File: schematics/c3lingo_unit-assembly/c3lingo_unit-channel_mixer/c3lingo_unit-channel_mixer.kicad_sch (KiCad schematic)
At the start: 83 parts, among them J301 Interconnect, J302 PowerSupply, J303 I/O, SW301 OnAir_X, SW302 Mute_X, U301 LM833-N, U302 LM339, U303 LM339, U304 LM339, U305 LM833-N

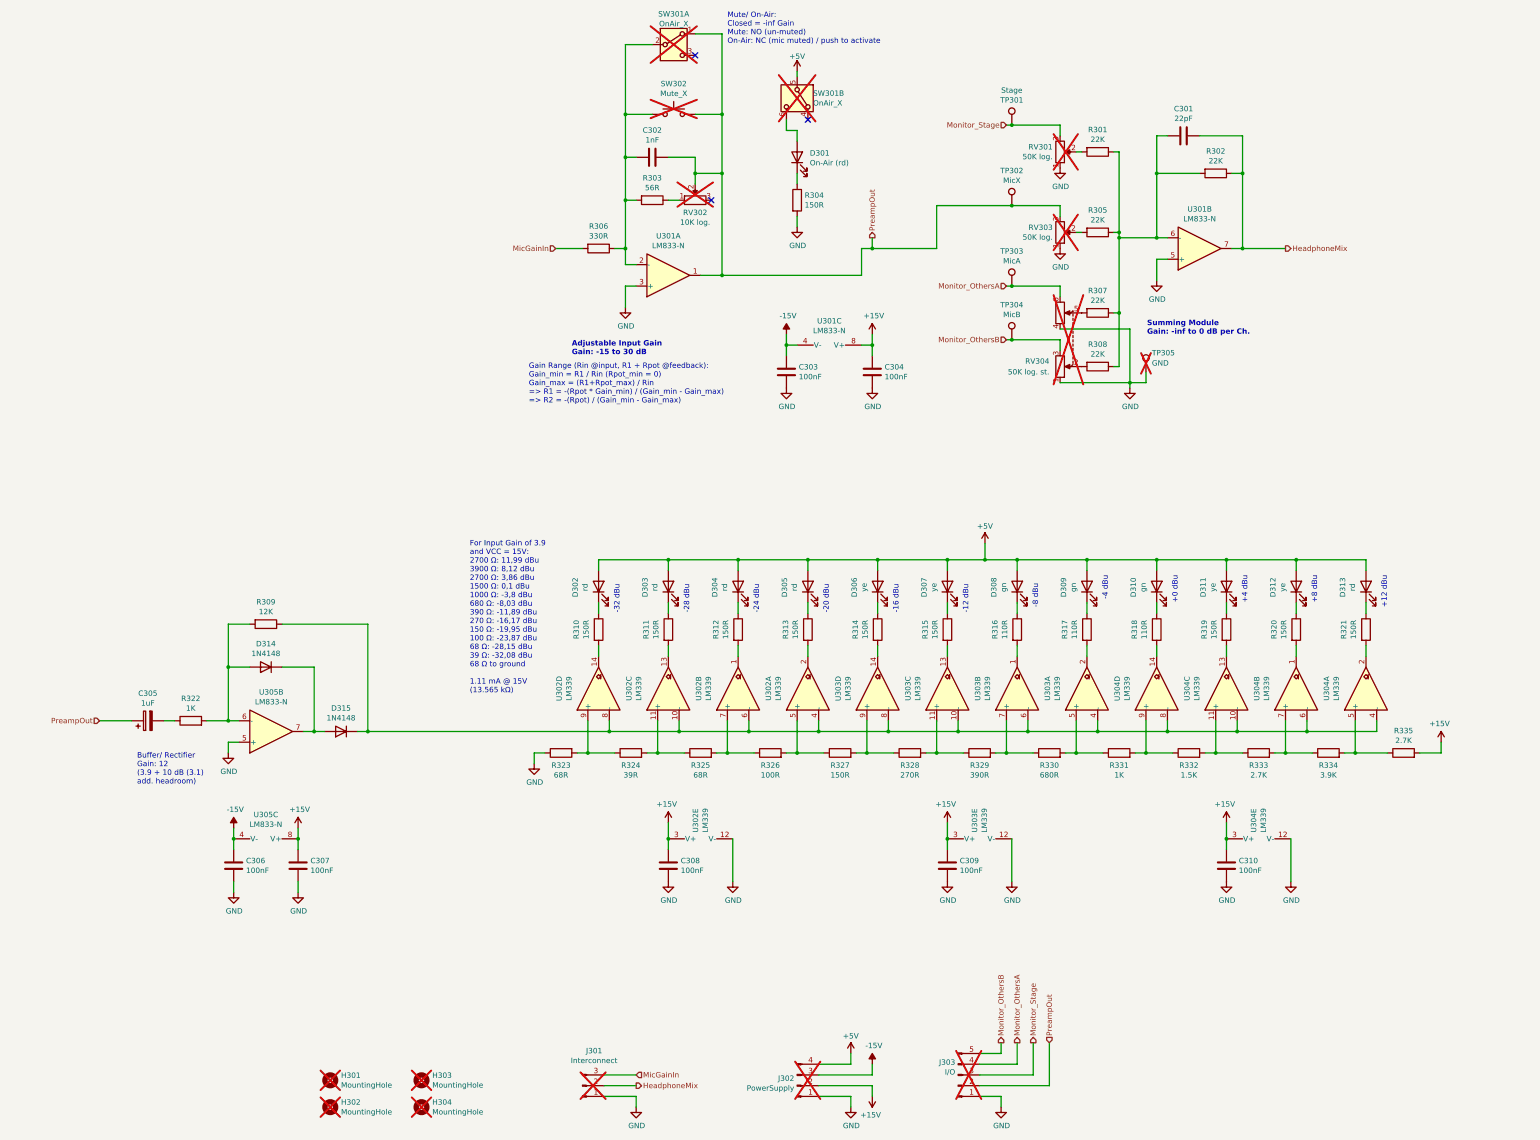
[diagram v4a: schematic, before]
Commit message: Tidy: Rename hierarchical labels
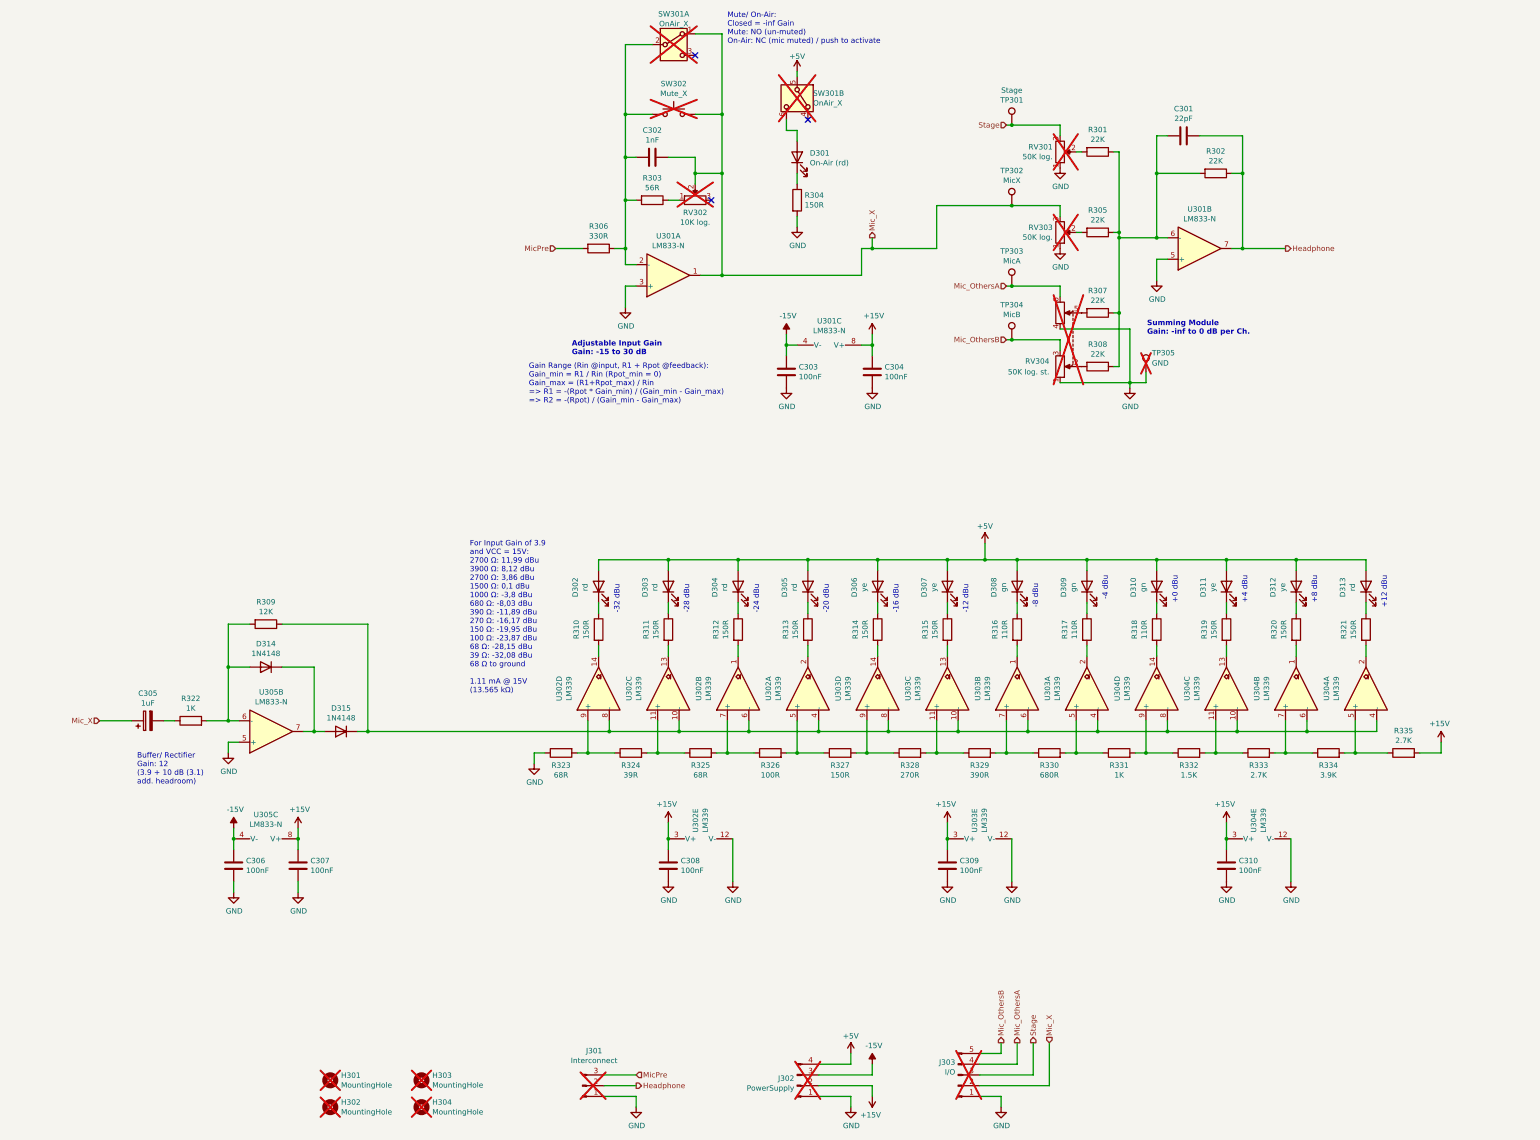
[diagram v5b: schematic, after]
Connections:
- net HeadphoneMix renamed Headphone
- net MicGainIn renamed MicPre
- net Monitor_OthersA renamed Mic_OthersA
- net Monitor_OthersB renamed Mic_OthersB
- net Monitor_Stage renamed Stage
- net PreampOut renamed Mic_X
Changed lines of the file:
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@@
 		)
 	)
-	(hierarchical_label "Monitor_OthersB"
+	(hierarchical_label "Mic_OthersB"
 		(shape output)
 		(at 251.46 264.16 90)
@@
 		)
 	)
-	(hierarchical_label "MicGainIn"
+	(hierarchical_label "MicPre"
 		(shape input)
 		(at 165.1 271.78 0)
@@
 		)
 	)
-	(hierarchical_label "PreampOut"
+	(hierarchical_label "Mic_X"
 		(shape input)
 		(at 38.1 187.96 180)
@@
 		)
 	)
-	(hierarchical_label "Monitor_Stage"
+	(hierarchical_label "Stage"
 		(shape input)
 		(at 252.73 46.99 180)
@@
 		)
 	)
-	(hierarchical_label "HeadphoneMix"
+	(hierarchical_label "Headphone"
 		(shape output)
 		(at 165.1 274.32 0)
@@
 		)
 	)
-	(hierarchical_label "Monitor_OthersA"
+	(hierarchical_label "Mic_OthersA"
 		(shape output)
 		(at 255.27 264.16 90)
@@
 		)
 	)
-	(hierarchical_label "MicGainIn"
+	(hierarchical_label "MicPre"
 		(shape input)
 		(at 146.05 76.2 180)
@@
 		)
 	)
-	(hierarchical_label "Monitor_OthersB"
+	(hierarchical_label "Mic_OthersB"
 		(shape input)
 		(at 252.73 97.79 180)
@@
 		)
 	)
-	(hierarchical_label "Monitor_OthersA"
+	(hierarchical_label "Mic_OthersA"
 		(shape input)
 		(at 252.73 85.09 180)
@@
 		)
 	)
-	(hierarchical_label "HeadphoneMix"
+	(hierarchical_label "Headphone"
 		(shape output)
 		(at 318.77 76.2 0)
@@
 		)
 	)
-	(hierarchical_label "PreampOut"
+	(hierarchical_label "Mic_X"
 		(shape output)
 		(at 220.98 73.66 90)
@@
 		)
 	)
-	(hierarchical_label "Monitor_Stage"
+	(hierarchical_label "Stage"
 		(shape output)
 		(at 259.08 264.16 90)
@@
 		)
 	)
-	(hierarchical_label "PreampOut"
+	(hierarchical_label "Mic_X"
 		(shape input)
 		(at 262.89 264.16 90)

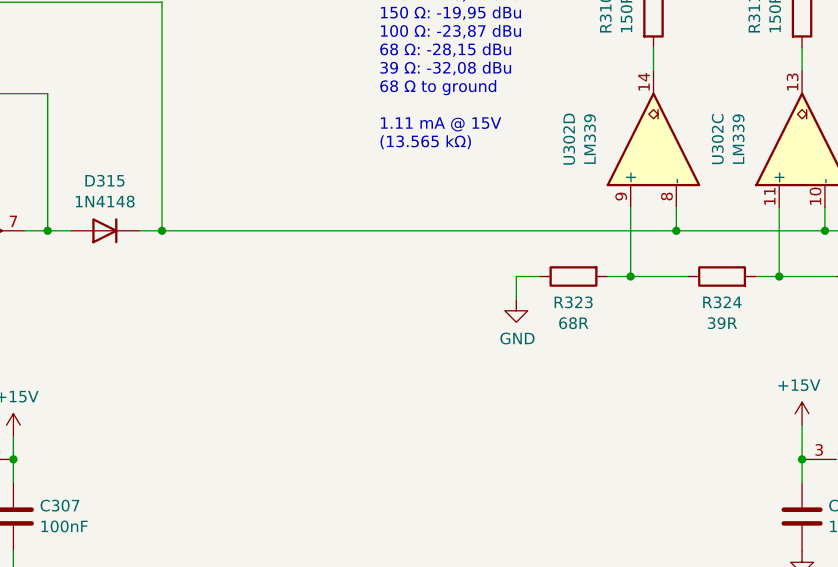
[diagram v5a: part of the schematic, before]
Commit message: Channel Mixer: Add LP filter to V/U meter
Note: schematic and dimenstions PDFs not updated as more changes come

To reduce HF noise on the power rail introduced by the switching of the comperators
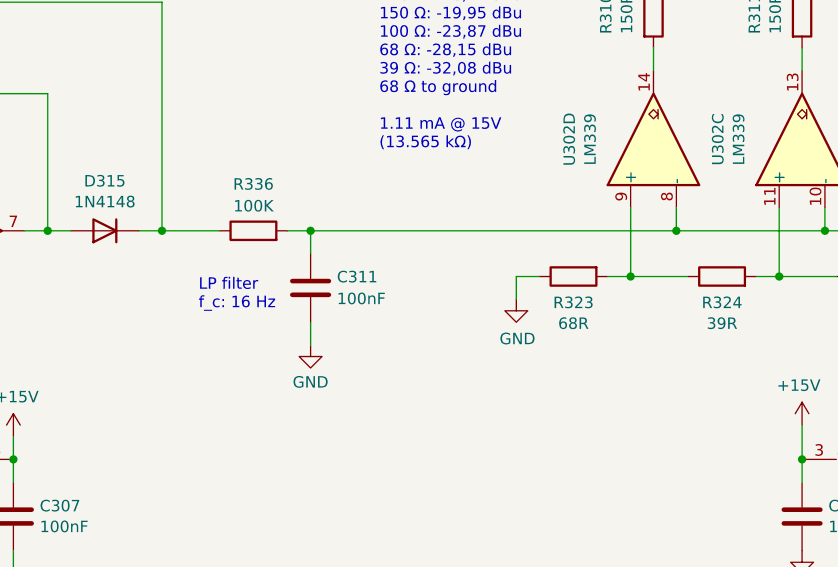
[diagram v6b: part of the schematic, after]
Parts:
- added C311: 100nF, Capacitor_SMD:C_0603_1608Metric_Pad1.08x0.95mm_HandSolder, symbol Device:C
- added R336: 100K, Resistor_SMD:R_0805_2012Metric_Pad1.20x1.40mm_HandSolder, symbol Device:R
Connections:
- net GND: now also C311.2
- net at U302.10 (-), U302.4 (-), U302.6 (-)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: now also C311.1, R336.2; no longer D315.1 (K), R309.1
- new net: D315.1 (K), R309.1, R336.1
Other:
- note added: "LP filter f_c: 16 Hz"

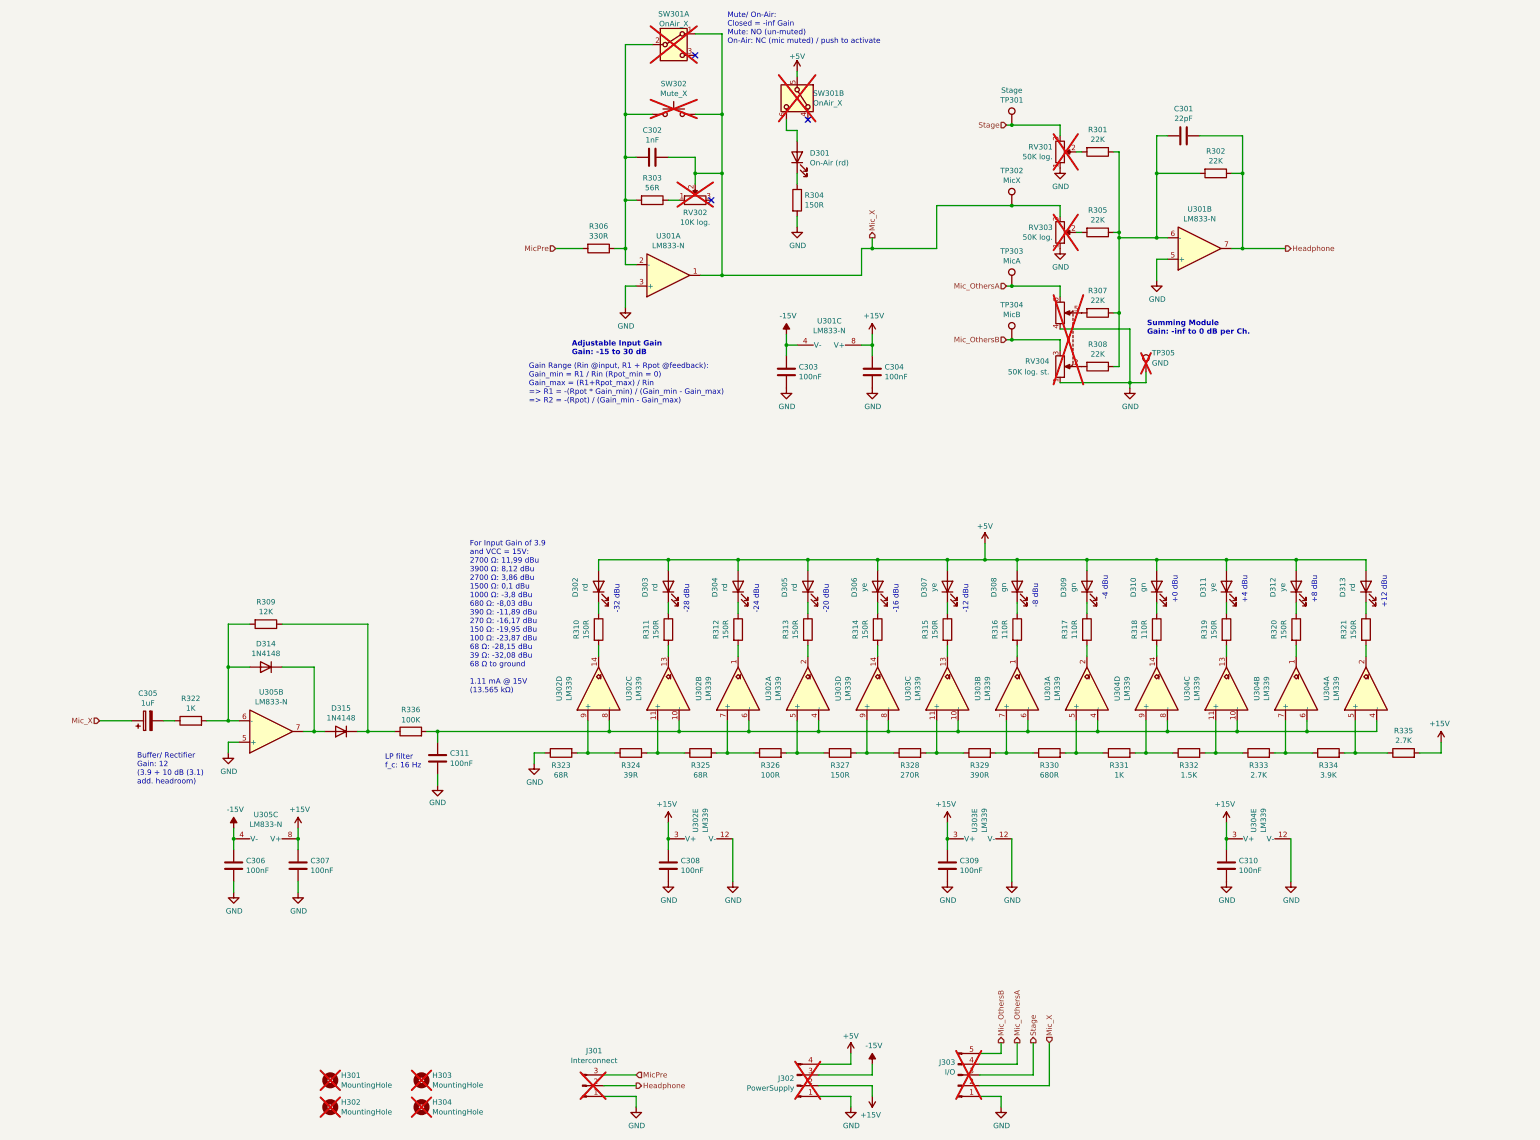
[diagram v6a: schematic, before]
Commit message: Channel Mixer: Rework muting mechanism
Note: Schematic PDF not updated yet
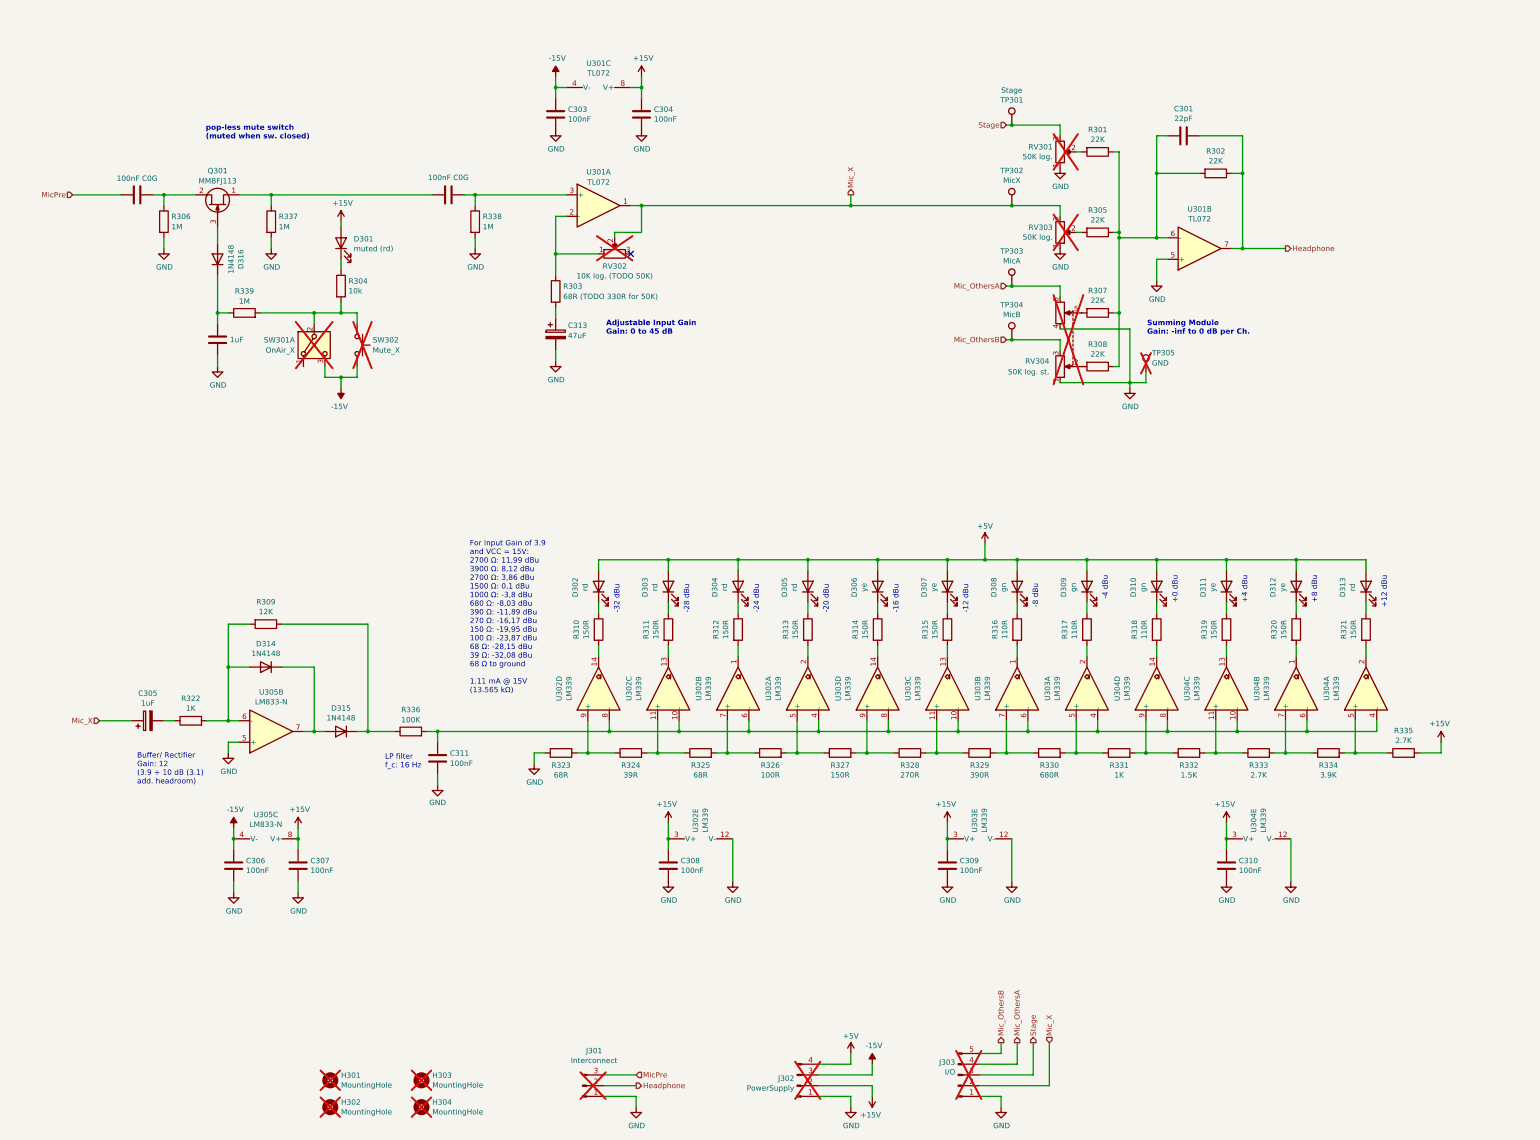
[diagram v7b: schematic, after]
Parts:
- removed unit 2 of SW301
- added C312: 100nF C0G, Capacitor_SMD:C_1206_3216Metric_Pad1.33x1.80mm_HandSolder, symbol Device:C
- added C313: 47uF, Capacitor_SMD:CP_Elec_6.3x5.4, symbol Device:C_Polarized
- added C314: 1uF, Capacitor_SMD:C_0603_1608Metric_Pad1.08x0.95mm_HandSolder, symbol Device:C
- added D316: 1N4148, Diode_SMD:D_SOD-123, symbol Device:D
- added Q301: MMBFJ113, Package_TO_SOT_SMD:SOT-23, symbol Transistor_FET:MMBFJ113
- added R337, R338, R339: 1M, Resistor_SMD:R_0805_2012Metric_Pad1.20x1.40mm_HandSolder, symbol Device:R
- C302: value 1nF -> 100nF C0G; footprint Capacitor_SMD:C_0603_1608Metric_Pad1.08x0.95mm_HandSolder -> Capacitor_SMD:C_1206_3216Metric_Pad1.33x1.80mm_HandSolder; LCSC Part # C1588 -> C97946
- C305: footprint Capacitor_SMD:C_Elec_4x5.8 -> Capacitor_SMD:CP_Elec_4x5.8
- D301: value On-Air (rd) -> muted (rd)
- R303: value 56R -> 68R (TODO 330R for 50K)
- R304: value 150R -> 10k
- R306: value 330R -> 1M
- RV302: value 10K log. -> 10K log. (TODO 50K)
- U301: value LM833-N -> TL072; symbol Amplifier_Operational:LM358 -> Amplifier_Operational:TL072; LCSC Part # C473907 -> C67473; Model LM833M or LM833MX (SOIC-8) -> TL072{C,HI,I}DR
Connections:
- net +15V: now also D301.2 (A)
- net -15V: now also SW301.3 (C), SW302.2
- net GND: now also R306.2, C313.2, C314.2, R337.2, R338.2; no longer R304.2, U301.3 (+)
- net MicPre: now also C302.2; no longer R306.2
- net Mic_X: no longer C302.1, SW301.1 (A), SW302.2
- net at R303.1, RV302.1: now also U301.2 (-)
- new net: C302.1, Q301.2 (S), R306.1
- new net: C312.1, R338.1, U301.3 (+)
- new net: C313.1, R303.2
- new net: R304.2, R339.2, SW301.2 (B), SW302.1
- new net: C312.2, Q301.1 (D), R337.1
- new net: D316.2 (A), Q301.3 (G)
- new net: C314.1, D316.1 (K), R339.1
- no-connect marks 3 -> 1
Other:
- note added: "Adjustable Input Gain Gain: 0 to 45 dB"
- note added: "pop-less mute switch (muted when sw. closed)"
- note removed: "Adjustable Input Gain Gain: -15 to 30 dB"
- note removed: "Gain Range (Rin @input, R1 + Rpot @feedback): Gain_min = R1 / Rin (Rpot_min = 0) Gain_max = (R1+Rpot_max) / Rin => R1 = -(Rpot * Gain_min) / (Gain_min - Gain_max) => R2 = -(Rpot) / (Gain_min - Gain_max)"
- note removed: "Mute/ On-Air: Closed = -inf Gain Mute: NO (un-muted) On-Air: NC (mic muted) / push to activate"
- moved on the sheet: C303, C304, D301, R303, R304, R306, RV302, SW301A, SW302, U301A, U301C
